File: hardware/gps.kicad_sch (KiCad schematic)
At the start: 1 part

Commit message: train schematics
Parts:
- added C? (x2): 0.1u, Capacitor_SMD:C_0603_1608Metric, symbol Device:C_Small
- added C? (x3): 4.7u, Capacitor_SMD:C_0805_2012Metric, symbol Device:C_Small
- added D? (x2): LED_Small_Filled, symbol Device:LED_Small_Filled
- added Q? (x2): BC847BDW1, Package_TO_SOT_SMD:SOT-363_SC-70-6, symbol Transistor_BJT:BC847BDW1
- added R? (x4): 22, Resistor_SMD:R_0603_1608Metric, symbol Device:R_Small
- added R?: 0, Resistor_SMD:R_0402_1005Metric, symbol Device:R_Small
- added R? (x2): 1k, Resistor_SMD:R_0603_1608Metric, symbol Device:R_Small
- added TP?: L96_RXD, symbol Connector:TestPoint
- added TP?: L96_TXD, symbol Connector:TestPoint
- added TP?: L96_GEO, symbol Connector:TestPoint
- added TP?: L96_JAM, symbol Connector:TestPoint
- added TP?: L96_SDA, symbol Connector:TestPoint
- added TP?: L96_SCL, symbol Connector:TestPoint
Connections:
- net GND: now reaches U?.10 (GND)
- net GND: now also U?.11 (GND), U?.12 (GND), U?.13 (GND), U?.14 (GND), U?.15 (GND), U?.18 (GND), U?.19 (GND), U?.21 (GND), U?.22 (GND), U?.27 (GND), U?.31 (GND), U?.4 (GND), U?.5 (GND), C?.2, C?.2, C?.2, C?.2, C?.2, Q?.1 (E1), Q?.4 (E2)
- net at U?.16 (RF_OUT): now also R?.1
- net at U?.17 (RF_IN): now also R?.2
- net L96_3DF: now reaches U?.2 (3D_FIX)
- net L96_3DF: now also Q?.2 (B1)
- net L96_JAM: now reaches U?.20 (JAM_IND)
- net L96_JAM: now also TP?.1
- net L96_GEO: now reaches U?.24 (GEO_FENCE)
- net L96_GEO: now also TP?.1
- net L96_TXD: now reaches U?.25 (TXD1)
- net L96_TXD: now also R?.1, TP?.1
- net L96_RXD: now reaches U?.26 (RXD1)
- net L96_RXD: now also R?.1, TP?.1
- net L96_1PPS: now reaches U?.29 (1PPS)
- net L96_1PPS: now also Q?.5 (B2)
- net L96_SDA: now reaches U?.3 (I2C_SDA)
- net L96_SDA: now also R?.1, TP?.1
- net L96_SCL: now reaches U?.6 (I2C_SCL)
- net L96_SCL: now also R?.1, TP?.1
- net VCC_BKUP_3V3: now reaches U?.8 (V_BCKP)
- net VCC_BKUP_3V3: now also C?.1, C?.1
- net VDD_AUX_3V3: now reaches U?.9 (VCC)
- net VDD_AUX_3V3: now also C?.1, C?.1, C?.1, R?.2, R?.2
- new net: D?.1 (K), Q?.3 (C2)
- new net: D?.2 (A), R?.1 (x2)
- new net: D?.1 (K), Q?.6 (C1)
- new net GPS_UART.RX: R?.2
- new net GPS_UART.TX: R?.2
- new net SENSOR_I2C.SCL: R?.2
- new net SENSOR_I2C.SDA: R?.2
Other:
- company: Erdapfel -> Frisius
- moved on the sheet: U?

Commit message: usb, charger, sensors, heir
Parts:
- removed Q? (x2): BC847BDW1, Package_TO_SOT_SMD:SOT-363_SC-70-6, symbol Transistor_BJT:BC847BDW1
- added Q? (x2): BC817W, Package_TO_SOT_SMD:SOT-323_SC-70, symbol Transistor_BJT:BC817W
- added TP? (x2): L96_JAM, symbol Connector:TestPoint
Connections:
- net GND: now also Q?.2 (E), Q?.2 (E)
- net L96_1PPS: now also Q?.1 (B), TP?.1
- net L96_3DF: now also Q?.1 (B), TP?.1
- net at D?.1 (K): now also Q?.3 (C) (x2)
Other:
- moved on the sheet: C?

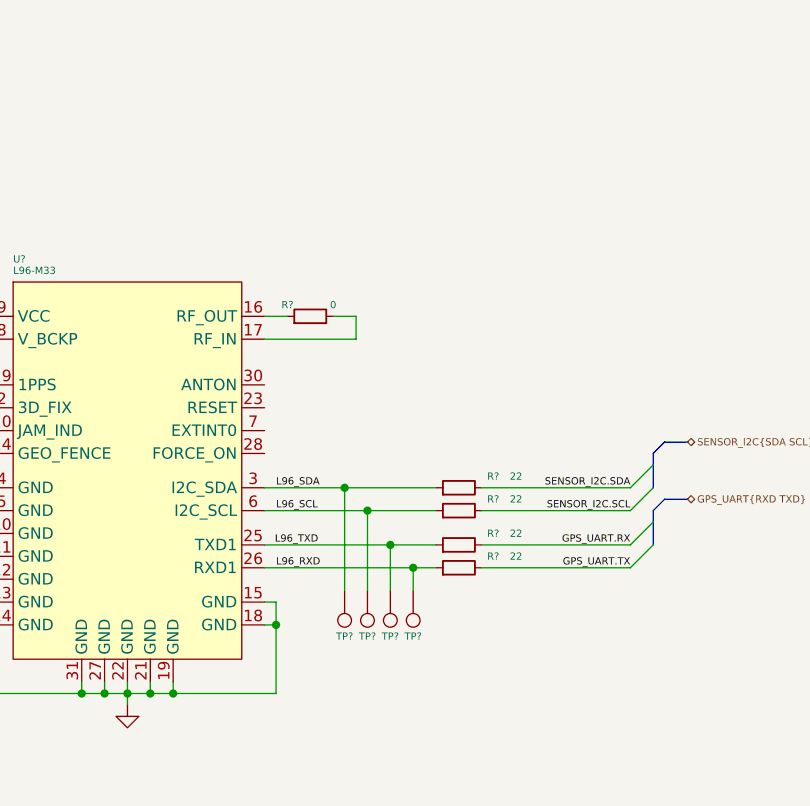
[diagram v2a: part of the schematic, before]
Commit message: usb, bms, proc, btn changes
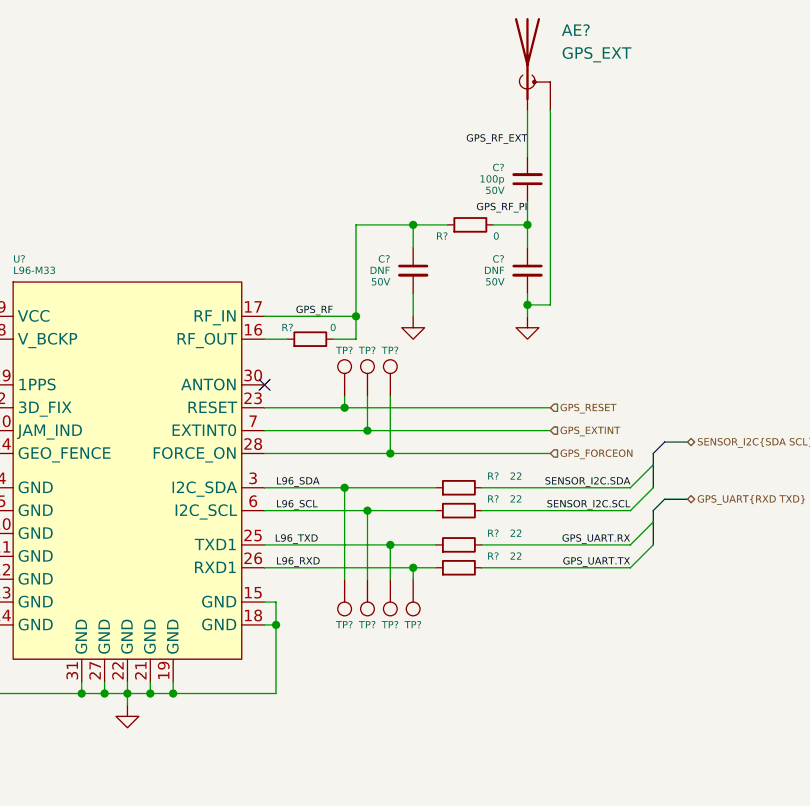
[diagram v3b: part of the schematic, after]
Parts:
- added AE?: GPS_EXT, Connector_Coaxial:U.FL_Hirose_U.FL-R-SMT-1_Vertical, symbol Device:Antenna_Shield
- added C? (x2): DNF, Capacitor_SMD:C_0402_1005Metric, symbol Device:C_Small
- added C?: 100p, Capacitor_SMD:C_0402_1005Metric, symbol Device:C_Small
- added R?: 0, Resistor_SMD:R_0402_1005Metric, symbol Device:R_Small
- added TP?: GPS_RESET, symbol Connector:TestPoint
- added TP?: GPS_EXTINT, symbol Connector:TestPoint
- added TP?: GPS_FORCE_ON, symbol Connector:TestPoint
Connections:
- net GND: now also AE?.2 (Shield), C?.2, C?.2
- net GPS_RF: now reaches R?.2, U?.17 (RF_IN)
- net GPS_RF: now also C?.1, R?.1
- net GPS_RESET: now reaches U?.23 (RESET)
- net GPS_RESET: now also TP?.1
- net GPS_FORCEON: now reaches U?.28 (FORCE_ON)
- net GPS_FORCEON: now also TP?.1
- net GPS_EXTINT: now reaches U?.7 (EXTINT0)
- net GPS_EXTINT: now also TP?.1
- new net GPS_RF_EXT: AE?.1 (A), C?.2
- new net GPS_RF_PI: C?.1, C?.1, R?.2
- no-connect marks 0 -> 1
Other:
- moved on the sheet: R?, TP?

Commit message: started b2b and power
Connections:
- net GPS_EXTINT: no longer names the net of TP?.1, U?.7 (EXTINT0)
- net GPS_FORCEON: no longer names the net of TP?.1, U?.28 (FORCE_ON)
- net GPS_RESET: no longer names the net of TP?.1, U?.23 (RESET)
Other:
- note added: "EXTINT0 pulled high internally, Enter standby via PMTK."
- note added: "FORCE_ON can float, enter backup via PMTK or disable VDD_AUX. Wake by cycling VDD_AUX."
- moved on the sheet: AE?, C?, D?, Q?, R?, TP?, U?

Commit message: checking footprint assignment, added current sense pac1934 for dev
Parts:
- D3, D4: renamed from D?; footprint (none) -> LED_SMD:LED_0603_1608Metric
- TP10, TP11, TP12, TP13, TP3, TP4, TP5, TP6, TP7, TP8, TP9: renamed from TP?; footprint (none) -> TestPoint:TestPoint_Pad_1.5x1.5mm
- U29: renamed from U?; footprint Module_GPS_bt:Quectel_L96-M33 -> bt_Module_GPS:Quectel_L96-M33
- gave numbers to parts that had none: 19

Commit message: hardware update
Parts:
- removed AE2: GPS_EXT, Connector_Coaxial:U.FL_Hirose_U.FL-R-SMT-1_Vertical, symbol Device:Antenna_Shield
- removed C43, C44: 4.7u, Capacitor_SMD:C_0805_2012Metric, symbol Device:C_Small
- removed C47, C49: DNF, Capacitor_SMD:C_0402_1005Metric, symbol Device:C_Small
- removed C48: 100p, Capacitor_SMD:C_0402_1005Metric, symbol Device:C_Small
- removed D4: LED_Small_Filled, LED_SMD:LED_0603_1608Metric, symbol Device:LED_Small_Filled
- removed Q4, Q5: BC817W, Package_TO_SOT_SMD:SOT-323_SC-70, symbol Transistor_BJT:BC817W
- removed R50: 1k, Resistor_SMD:R_0603_1608Metric, symbol Device:R_Small
- removed R56: 0, Resistor_SMD:R_0402_1005Metric, symbol Device:R_Small
- removed TP10: L96_SCL, TestPoint:TestPoint_Pad_1.5x1.5mm, symbol Connector:TestPoint
- removed TP11: GPS_FORCE_ON, TestPoint:TestPoint_Pad_1.5x1.5mm, symbol Connector:TestPoint
- removed TP12: L96_TXD, TestPoint:TestPoint_Pad_1.5x1.5mm, symbol Connector:TestPoint
- removed TP13: L96_RXD, TestPoint:TestPoint_Pad_1.5x1.5mm, symbol Connector:TestPoint
- removed TP3, TP4, TP5: L96_JAM, TestPoint:TestPoint_Pad_1.5x1.5mm, symbol Connector:TestPoint
- removed TP6: L96_GEO, TestPoint:TestPoint_Pad_1.5x1.5mm, symbol Connector:TestPoint
- removed TP7: GPS_RESET, TestPoint:TestPoint_Pad_1.5x1.5mm, symbol Connector:TestPoint
- removed TP8: L96_SDA, TestPoint:TestPoint_Pad_1.5x1.5mm, symbol Connector:TestPoint
- removed TP9: GPS_EXTINT, TestPoint:TestPoint_Pad_1.5x1.5mm, symbol Connector:TestPoint
- added TP1: L96_FIX, TestPoint:TestPoint_Pad_D1.0mm, symbol Connector:TestPoint
- C17: renamed from C45; footprint Capacitor_SMD:C_0603_1608Metric -> Capacitor_SMD:C_0402_1005Metric
- C18: renamed from C42; footprint Capacitor_SMD:C_0805_2012Metric -> Capacitor_SMD:C_0603_1608Metric
- C19: renamed from C46; footprint Capacitor_SMD:C_0603_1608Metric -> Capacitor_SMD:C_0402_1005Metric
- R10: renamed from R55; footprint Resistor_SMD:R_0603_1608Metric -> Resistor_SMD:R_0402_1005Metric
- R5: renamed from R49; footprint Resistor_SMD:R_0603_1608Metric -> Resistor_SMD:R_0402_1005Metric
- R7: renamed from R52; footprint Resistor_SMD:R_0603_1608Metric -> Resistor_SMD:R_0402_1005Metric
- R8: renamed from R53; footprint Resistor_SMD:R_0603_1608Metric -> Resistor_SMD:R_0402_1005Metric
- R9: renamed from R54; footprint Resistor_SMD:R_0603_1608Metric -> Resistor_SMD:R_0402_1005Metric
- renumbered D3 to D1, R51 to R6, U29 to U4
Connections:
- net GND: now also D1.1 (K)
- net GPS_RF: now also R6.1; no longer R6.2
- net L96_1PPS: now also R5.2
- net VDD_AUX_3V3: no longer R5.2
- net at U4.16 (RF_OUT): now also R6.2; no longer R6.1
- net L96_3DF: no longer names the net of U4.2 (3D_FIX)
- net L96_3DF: now also TP1.1
- net L96_GEO: no longer names the net of U4.24 (GEO_FENCE)
- net L96_JAM: no longer names the net of U4.20 (JAM_IND)
- no-connect marks 1 -> 6
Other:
- note added: "Shouldn´t need reset."
- moved on the sheet: C17, C18, C19, D1, R10, R5, R6, R7, R8, R9

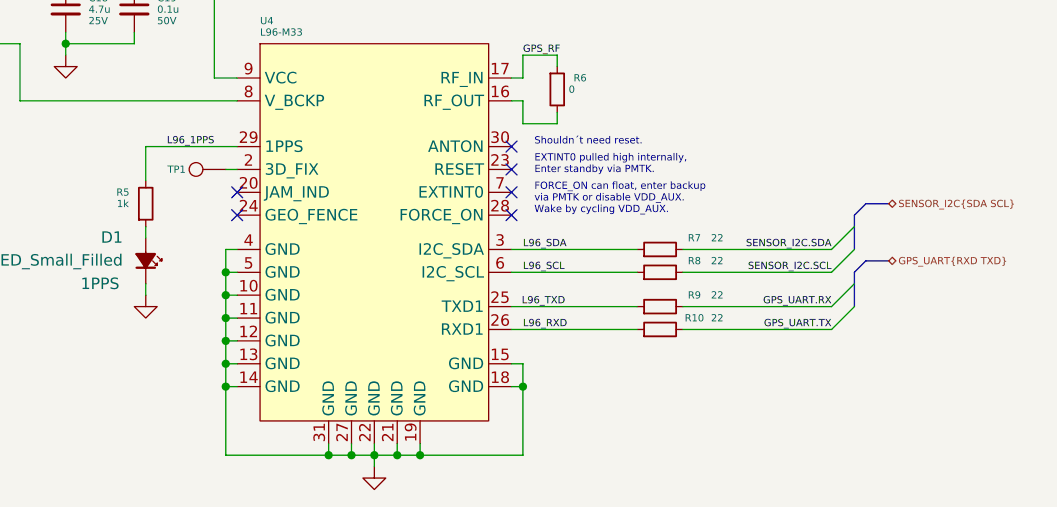
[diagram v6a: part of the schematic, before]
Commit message: initial component placement and design simplification
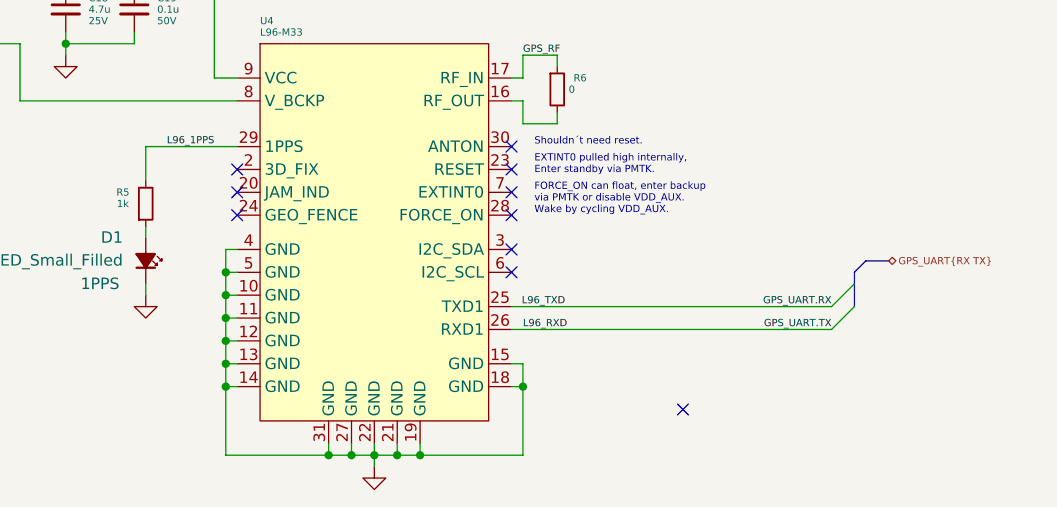
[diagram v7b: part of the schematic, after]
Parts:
- removed R10, R7, R8, R9: 22, Resistor_SMD:R_0402_1005Metric, symbol Device:R_Small
- removed TP1: L96_FIX, TestPoint:TestPoint_Pad_D1.0mm, symbol Connector:TestPoint
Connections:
- net L96_RXD is gone; now on net GPS_UART.TX: U4.26 (RXD1)
- net L96_TXD is gone; now on net GPS_UART.RX: U4.25 (TXD1)
- net L96_SCL: no longer names the net of U4.6 (I2C_SCL)
- net L96_SDA: no longer names the net of U4.3 (I2C_SDA)
- no-connect marks 6 -> 10
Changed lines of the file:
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@@
   (junction (at 125.73 68.58) (diameter 0) (color 0 0 0 0)
   )
+  (no_connect (at 137.16 90.17))
   (no_connect (at 167.64 87.63))
   (no_connect (at 137.16 95.25))
@@
   (no_connect (at 167.64 92.71))
   (no_connect (at 167.64 95.25))
-  (bus_entry (at 203.2 99.06) (size 2.54 -2.54)
-    (stroke (width 0) (type default) (color 0 0 0 0))
-  )
+  (no_connect (at 167.64 99.06))
+  (no_connect (at 167.64 101.6))
+  (no_connect (at 186.69 116.84))
   (bus_entry (at 203.2 107.95) (size 2.54 -2.54)
     (stroke (width 0) (type default) (color 0 0 0 0))
   )
-  (bus_entry (at 203.2 101.6) (size 2.54 -2.54)
-    (stroke (width 0) (type default) (color 0 0 0 0))
-  )
   (bus_entry (at 203.2 105.41) (size 2.54 -2.54)
     (stroke (width 0) (type default) (color 0 0 0 0))
   )
-  (wire (pts (xy 135.89 90.17) (xy 137.16 90.17))
-    (stroke (width 0) (type default) (color 0 0 0 0))
-  )
   (wire (pts (xy 168.91 85.09) (xy 172.72 85.09))
     (stroke (width 0) (type default) (color 0 0 0 0))
@@
     (stroke (width 0) (type default) (color 0 0 0 0))
   )
-  (wire (pts (xy 186.69 101.6) (xy 203.2 101.6))
-    (stroke (width 0) (type default) (color 0 0 0 0))
-  )
   (wire (pts (xy 135.89 99.06) (xy 135.89 101.6))
     (stroke (width 0) (type default) (color 0 0 0 0))
@@
     (stroke (width 0) (type default) (color 0 0 0 0))
   )
-  (wire (pts (xy 167.64 99.06) (xy 181.61 99.06))
-    (stroke (width 0) (type default) (color 0 0 0 0))
-  )
   (wire (pts (xy 118.11 76.2) (xy 125.73 76.2))
     (stroke (width 0) (type default) (color 0 0 0 0))
@@
     (stroke (width 0) (type default) (color 0 0 0 0))
   )
-  (bus (pts (xy 205.74 96.52) (xy 205.74 99.06))
-    (stroke (width 0) (type default) (color 0 0 0 0))
-  )
   (wire (pts (xy 152.4 121.92) (xy 152.4 120.65))
     (stroke (width 0) (type default) (color 0 0 0 0))
   )
-  (wire (pts (xy 186.69 99.06) (xy 203.2 99.06))
-    (stroke (width 0) (type default) (color 0 0 0 0))
-  )
   (wire (pts (xy 168.91 114.3) (xy 168.91 111.76))
     (stroke (width 0) (type default) (color 0 0 0 0))
@@
     (stroke (width 0) (type default) (color 0 0 0 0))
   )
-  (wire (pts (xy 186.69 105.41) (xy 203.2 105.41))
-    (stroke (width 0) (type default) (color 0 0 0 0))
-  )
   (wire (pts (xy 135.89 114.3) (xy 137.16 114.3))
     (stroke (width 0) (type default) (color 0 0 0 0))
@@
     (stroke (width 0) (type default) (color 0 0 0 0))
   )
-  (wire (pts (xy 203.2 107.95) (xy 186.69 107.95))
+  (wire (pts (xy 167.64 107.95) (xy 203.2 107.95))
     (stroke (width 0) (type default) (color 0 0 0 0))
   )
@@
     (stroke (width 0) (type default) (color 0 0 0 0))
   )
-  (bus (pts (xy 205.74 95.25) (xy 205.74 96.52))
-    (stroke (width 0) (type default) (color 0 0 0 0))
-  )
   (wire (pts (xy 135.89 111.76) (xy 137.16 111.76))
     (stroke (width 0) (type default) (color 0 0 0 0))
@@
     (stroke (width 0) (type default) (color 0 0 0 0))
   )
-  (wire (pts (xy 167.64 107.95) (xy 181.61 107.95))
-    (stroke (width 0) (type default) (color 0 0 0 0))
-  )
   (wire (pts (xy 125.73 74.93) (xy 125.73 76.2))
     (stroke (width 0) (type default) (color 0 0 0 0))
@@
     (stroke (width 0) (type default) (color 0 0 0 0))
   )
-  (wire (pts (xy 167.64 105.41) (xy 181.61 105.41))
+  (wire (pts (xy 167.64 105.41) (xy 203.2 105.41))
     (stroke (width 0) (type default) (color 0 0 0 0))
   )
@@
     (stroke (width 0) (type default) (color 0 0 0 0))
   )
-  (bus (pts (xy 207.01 93.98) (xy 209.55 93.98))
-    (stroke (width 0) (type default) (color 0 0 0 0))
-  )
   (wire (pts (xy 135.89 104.14) (xy 135.89 106.68))
     (stroke (width 0) (type default) (color 0 0 0 0))
@@
     (stroke (width 0) (type default) (color 0 0 0 0))
   )
-  (wire (pts (xy 167.64 101.6) (xy 181.61 101.6))
-    (stroke (width 0) (type default) (color 0 0 0 0))
-  )
   (wire (pts (xy 147.32 121.92) (xy 147.32 120.65))
     (stroke (width 0) (type default) (color 0 0 0 0))
@@
   )
   (wire (pts (xy 118.11 67.31) (xy 118.11 68.58))
-    (stroke (width 0) (type default) (color 0 0 0 0))
-  )
-  (bus (pts (xy 205.74 95.25) (xy 207.01 93.98))
     (stroke (width 0) (type default) (color 0 0 0 0))
   )
@@
     (effects (font (size 0.8 0.8)) (justify left bottom))
   )
-  (label "SENSOR_I2C.SCL" (at 203.2 101.6 180)
-    (effects (font (size 0.8 0.8)) (justify right bottom))
-  )
-  (label "L96_SCL" (at 168.91 101.6 0)
-    (effects (font (size 0.8 0.8)) (justify left bottom))
-  )
   (label "L96_1PPS" (at 134.62 87.63 180)
     (effects (font (size 0.8 0.8)) (justify right bottom))
@@
     (effects (font (size 0.8 0.8)) (justify right bottom))
   )
-  (label "L96_SDA" (at 168.91 99.06 0)
-    (effects (font (size 0.8 0.8)) (justify left bottom))
-  )
   (label "GPS_UART.RX" (at 203.2 105.41 180)
     (effects (font (size 0.8 0.8)) (justify right bottom))
@@
     (effects (font (size 0.8 0.8)) (justify left bottom))
   )
-  (label "SENSOR_I2C.SDA" (at 203.2 99.06 180)
-    (effects (font (size 0.8 0.8)) (justify right bottom))
-  )
   (label "L96_TXD" (at 168.778 105.41 0)
     (effects (font (size 0.8 0.8)) (justify left bottom))
   )
-  (hierarchical_label "GPS_UART{RXD TXD}" (shape bidirectional) (at 209.55 100.33 0)
+  (hierarchical_label "GPS_UART{RX TX}" (shape bidirectional) (at 209.55 100.33 0)
     (effects (font (size 0.8 0.8)) (justify left))
   )
-  (hierarchical_label "SENSOR_I2C{SDA SCL}" (shape bidirectional) (at 209.55 93.98 0)
-    (effects (font (size 0.8 0.8)) (justify left))
-  )
   (symbol (lib_id "Device:C_Small") (at 125.73 72.39 0) (unit 1)
     (in_bom yes) (on_board yes)
@@
     (property "Voltage" "50V" (id 4) (at 128.27 73.66 0)
       (effects (font (size 0.8 0.8)) (justify left))
-    )
-    (pin "1")
-    (pin "2")
-  )
-  (symbol (lib_id "Device:R_Small") (at 184.15 107.95 90) (unit 1)
-    (in_bom yes) (on_board yes)
-    (property "Reference" "R10" (id 0) (at 187.96 106.68 90)
-      (effects (font (size 0.8 0.8)))
-    )
-    (property "Value" "22" (id 1) (at 190.5 106.68 90)
-      (effects (font (size 0.8 0.8)))
-    )
-    (property "Footprint" "Resistor_SMD:R_0402_1005Metric" (id 2) (at 184.15 107.95 0)
-      (effects (font (size 0.8 0.8)) hide)
-    )
-    (property "Datasheet" "~" (id 3) (at 184.15 107.95 0)
-      (effects (font (size 0.8 0.8)) hide)
     )
     (pin "1")
@@
     (pin "2")
   )
-  (symbol (lib_id "Device:R_Small") (at 184.15 99.06 90) (unit 1)
-    (in_bom yes) (on_board yes)
-    (property "Reference" "R7" (id 0) (at 187.96 97.79 90)
-      (effects (font (size 0.8 0.8)))
-    )
-    (property "Value" "22" (id 1) (at 190.5 97.79 90)
-      (effects (font (size 0.8 0.8)))
-    )
-    (property "Footprint" "Resistor_SMD:R_0402_1005Metric" (id 2) (at 184.15 99.06 0)
-      (effects (font (size 0.8 0.8)) hide)
-    )
-    (property "Datasheet" "~" (id 3) (at 184.15 99.06 0)
-      (effects (font (size 0.8 0.8)) hide)
-    )
-    (pin "1")
-    (pin "2")
-  )
   (symbol (lib_id "power:GND") (at 118.11 77.47 0) (unit 1)
     (in_bom yes) (on_board yes) (fields_autoplaced)
@@
     (pin "2")
   )
-  (symbol (lib_id "Device:R_Small") (at 184.15 105.41 90) (unit 1)
-    (in_bom yes) (on_board yes)
-    (property "Reference" "R9" (id 0) (at 187.96 104.14 90)
-      (effects (font (size 0.8 0.8)))
-    )
-    (property "Value" "22" (id 1) (at 190.5 104.14 90)
-      (effects (font (size 0.8 0.8)))
-    )
-    (property "Footprint" "Resistor_SMD:R_0402_1005Metric" (id 2) (at 184.15 105.41 0)
-      (effects (font (size 0.8 0.8)) hide)
-    )
-    (property "Datasheet" "~" (id 3) (at 184.15 105.41 0)
-      (effects (font (size 0.8 0.8)) hide)
-    )
-    (pin "1")
-    (pin "2")
-  )
   (symbol (lib_id "bt_power:VDD_AUX_3V3") (at 118.11 67.31 0) (unit 1)
     (in_bom no) (on_board no)
@@
     (pin "2")
   )
-  (symbol (lib_id "Device:R_Small") (at 184.15 101.6 90) (unit 1)
-    (in_bom yes) (on_board yes)
-    (property "Reference" "R8" (id 0) (at 187.96 100.33 90)
-      (effects (font (size 0.8 0.8)))
-    )
-    (property "Value" "22" (id 1) (at 190.5 100.33 90)
-      (effects (font (size 0.8 0.8)))
-    )
-    (property "Footprint" "Resistor_SMD:R_0402_1005Metric" (id 2) (at 184.15 101.6 0)
-      (effects (font (size 0.8 0.8)) hide)
-    )
-    (property "Datasheet" "~" (id 3) (at 184.15 101.6 0)
-      (effects (font (size 0.8 0.8)) hide)
-    )
-    (pin "1")
-    (pin "2")
-  )
   (symbol (lib_id "power:GND") (at 104.14 83.82 0) (unit 1)
     (in_bom yes) (on_board yes) (fields_autoplaced)
@@
       (effects (font (size 1.27 1.27)) hide)
     )
-    (pin "1")
-  )
-  (symbol (lib_id "Connector:TestPoint") (at 135.89 90.17 90) (unit 1)
-    (in_bom yes) (on_board yes)
-    (property "Reference" "TP1" (id 0) (at 131.445 90.17 90)
-      (effects (font (size 0.8 0.8)) (justify left))
-    )
-    (property "Value" "L96_FIX" (id 1) (at 133.35 87.63 0)
-      (effects (font (size 0.8 0.8)) (justify left) hide)
-    )
-    (property "Footprint" "TestPoint:TestPoint_Pad_D1.0mm" (id 2) (at 135.89 85.09 0)
-      (effects (font (size 1.27 1.27)) hide)
-    )
-    (property "Datasheet" "~" (id 3) (at 135.89 85.09 0)
-      (effects (font (size 1.27 1.27)) hide)
-    )

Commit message: fixing submodule
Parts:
- added R23, R27: 0, Resistor_SMD:R_0402_1005Metric, symbol Device:R_Small
- added TP11, TP12, TP13, TP14: GPS_3DF, symbol Connector:TestPoint
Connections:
- net at U4.2 (3D_FIX): now also TP11.1
- net at U4.23 (RESET): now also TP12.1
- net at U4.28 (FORCE_ON): now also TP14.1
- net at U4.3 (I2C_SDA): now also R23.1
- net at U4.6 (I2C_SCL): now also R27.1
- net at U4.7 (EXTINT0): now also TP13.1
- new net SENSOR_I2C.SCL: R27.2
- new net SENSOR_I2C.SDA: R23.2
- no-connect marks 10 -> 4
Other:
- moved on the sheet: D1, R5
